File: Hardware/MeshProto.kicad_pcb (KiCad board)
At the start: 2 copper layers, 30.2 x 31.6 mm, 103 parts, among them P1 CONN_1, P10 CONN_1, P11 CONN_1, P12 CONN_1, P13 CONN_1, P14 CONN_1, P15 CONN_1, P16 CONN_1, P17 CONN_1, P18 CONN_1, P19 CONN_1, P2 CONN_1, P20 CONN_1, P21 CONN_1, P22 CONN_1, P23 CONN_1, P24 CONN_1, P25 CONN_1, P26 CONN_1, P27 CONN_1, P28 CONN_1, P29 CONN_1, P3 CONN_1, P30 CONN_1, P31 CONN_1, P32 CONN_1, P33 CONN_1, P34 CONN_1, P35 CONN_1, P36 CONN_1, P37 CONN_1, P38 CONN_1, P39 CONN_1, P4 CONN_1, P40 CONN_1, P41 CONN_1, P42 CONN_1, P43 CONN_1, P44 CONN_1, P45 CONN_1, P46 CONN_1, P47 CONN_1, P48 CONN_1, P49 CONN_1, P5 CONN_1, P50 CONN_1, P51 CONN_1, P52 CONN_1, P53 CONN_1, P54 CONN_1, P55 CONN_1, P56 CONN_1, P57 CONN_1, P58 CONN_1, P59 CONN_1, P6 CONN_1, P60 CONN_1, P61 CONN_1, P62 CONN_1, P63 CONN_1, P64 CONN_1, P65 CONN_1, P66 CONN_1, P67 CONN_1, P68 CONN_1, P69 CONN_1, P7 CONN_1, P70 CONN_1, P71 CONN_1, P72 CONN_1, P73 CONN_1, P74 CONN_1, P75 CONN_1, P76 CONN_1, P77 CONN_1, P78 CONN_1, P79 CONN_1, P8 CONN_1, P80 CONN_1, P81 CONN_1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

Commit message: Further minor changes.
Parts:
- moved SW1 3.82 mm to (134.7, 113.0), turned to 90 degrees
- moved P82 0.95 mm to (134.7, 108.3)
- moved P81 0.09 mm to (134.7, 106.7)
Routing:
- net N-0000052: track 8.81 -> 7.91 mm
- net GND: track 52.6 -> 53.5 mm
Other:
- board text added: "MeshProto v1.0 ©David Chanter, Bob Powers, Andy Gelme"
- board text added: "Reset"
- board text added: "This Way"
- board text removed: "MeshProto v1.0 © David Chanter, Bob Powers, Andy Gelme"
- board text removed: "This Way Up"
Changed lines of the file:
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@@
-(kicad_pcb (version 3) (host pcbnew "(2013-11-13 BZR 4466)-product")
+(kicad_pcb (version 3) (host pcbnew "(2013-11-20 BZR 4495)-product")
   (general
     (links 36)
-    (no_connects 1)
-    (area 131.413229 96.5166 165.135343 130.6954)
+    (no_connects 0)
+    (area 129.261801 96.5166 165.135343 130.6954)
     (thickness 1.6)
-    (drawings 31)
+    (drawings 32)
     (tracks 80)
     (zones 0)
@@
     (18 B.Paste user)
     (19 F.Paste user)
-    (20 B.SilkS user)
+    (20 B.SilkS user hide)
     (21 F.SilkS user)
     (22 B.Mask user)
@@
   )
   (setup
-    (last_trace_width 0.3048)
+    (last_trace_width 0.2032)
     (user_trace_width 0.3048)
     (trace_clearance 0.2032)
@@
   )
   (module _MT_TC007-TactileSwitch (layer F.Cu)
-    (at 134.71 116.82 270)
-    (fp_text reference SW1 (at -2.04 0 360) (layer F.SilkS)
+    (at 134.71 113.004 90)
+    (fp_text reference SW1 (at -2.04 0 180) (layer F.SilkS)
       (effects (font (size 0.75 0.75) (thickness 0.15)))
     )
-    (fp_text value SPST (at -0.01 -2.42 270) (layer F.SilkS) hide
+    (fp_text value SPST (at -0.01 -2.42 90) (layer F.SilkS) hide
       (effects (font (size 1.5 1.5) (thickness 0.15)))
     )
@@
     (fp_line (start -1.95 -1.45) (end 1.95 -1.45) (layer F.SilkS) (width 0.15))
     (fp_line (start 1.95 -1.45) (end 1.95 -0.73) (layer F.SilkS) (width 0.15))
-    (pad 1 smd rect (at -2.05 0 270) (size 0.9 1.3) (layers F.Cu F.Paste F.Mask)
+    (pad 1 smd rect (at -2.05 0 90) (size 0.9 1.3) (layers F.Cu F.Paste F.Mask)
       (net 3 N-0000052))
-    (pad 2 smd rect (at 2.05 0 270) (size 0.9 1.3) (layers F.Cu F.Paste F.Mask)
+    (pad 2 smd rect (at 2.05 0 90) (size 0.9 1.3) (layers F.Cu F.Paste F.Mask)
       (net 2 GND))
-    (pad "" thru_hole rect (at 0 0.9 270) (size 0.7 0.7) (drill 0.7) (layers *.Cu *.Mask F.SilkS))
-    (pad "" thru_hole rect (at -0.01 -0.9 270) (size 0.7 0.7) (drill 0.7) (layers *.Cu *.Mask F.SilkS))
-  )
-  (module _MP_1Pin (layer F.Cu)
-    (at 134.62 106.68)
+    (pad "" thru_hole rect (at 0 0.9 90) (size 0.7 0.7) (drill 0.7) (layers *.Cu *.Mask F.SilkS))
+    (pad "" thru_hole rect (at -0.01 -0.9 90) (size 0.7 0.7) (drill 0.7) (layers *.Cu *.Mask F.SilkS))
+  )
+  (module _MP_1Pin (layer F.Cu)
+    (at 134.71 106.68)
     (fp_text reference P81 (at 0 0) (layer F.SilkS) hide
       (effects (font (size 1 1) (thickness 0.15)))
@@
       (effects (font (size 1 1) (thickness 0.15)))
     )
-    (pad 1 thru_hole circle (at 0 0) (size 1.85928 1.85928) (drill 0.8128) (layers *.Cu *.Mask F.SilkS)
+    (pad 1 thru_hole circle (at 0 -0.946) (size 1.85928 1.85928) (drill 0.8128) (layers *.Cu *.Mask F.SilkS)
       (net 1 BAT+))
   )
   (module _MP_1Pin (layer F.Cu)
-    (at 134.62 109.22)
+    (at 134.71 108.274)
     (fp_text reference P82 (at 0 0) (layer F.SilkS) hide
       (effects (font (size 1 1) (thickness 0.15)))
@@
       (xy -0.75692 1.12268)) (layer F.SilkS) (width 0.00254))
   )
-  (gr_text meshthing.com (at 162.052 113.538 90) (layer B.SilkS)
-    (effects (font (size 1.5 1.5) (thickness 0.3)) (justify mirror))
-  )
-  (gr_text "MeshProto v1.0\n© David Chanter, Bob Powers,\nAndy Gelme" (at 161.3408 117.5766 90) (layer F.SilkS)
+  (gr_text Reset (at 134.71 116.11) (layer F.SilkS)
+    (effects (font (size 0.5 0.5) (thickness 0.125)))
+  )
+  (gr_text meshthing.com (at 162.08 115.87 90) (layer F.SilkS)
+    (effects (font (size 1.5 1.5) (thickness 0.3)))
+  )
+  (gr_text "MeshProto v1.0\n©David Chanter, Bob Powers,\nAndy Gelme" (at 161.3408 103.62 90) (layer B.SilkS)
+    (effects (font (size 0.5 0.5) (thickness 0.1)) (justify left mirror))
+  )
+  (gr_text ↑ (at 162.8394 106.35) (layer F.SilkS)
+    (effects (font (size 1.5 1.5) (thickness 0.3)))
+  )
+  (gr_line (start 162.56 103.6938) (end 161.8742 103.6938) (angle 90) (layer F.SilkS) (width 0.2))
+  (gr_line (start 161.3662 104.2018) (end 161.8234 103.7446) (angle 90) (layer F.SilkS) (width 0.2))
+  (gr_line (start 161.3662 105.4718) (end 161.3662 104.2018) (angle 90) (layer F.SilkS) (width 0.2))
+  (gr_line (start 163.0426 105.4718) (end 161.3662 105.4718) (angle 90) (layer F.SilkS) (width 0.2))
+  (gr_line (start 163.0426 104.1764) (end 163.0426 105.4718) (angle 90) (layer F.SilkS) (width 0.2))
+  (gr_line (start 162.56 103.6938) (end 163.0426 104.1764) (angle 90) (layer F.SilkS) (width 0.2))
+  (gr_text "This\nWay" (at 161.6456 106.45) (layer F.SilkS)
     (effects (font (size 0.5 0.5) (thickness 0.1)))
   )
-  (gr_text ↑ (at 162.8394 107.4928) (layer F.SilkS)
-    (effects (font (size 1.5 1.5) (thickness 0.3)))
-  )
-  (gr_line (start 162.56 104.0638) (end 161.8742 104.0638) (angle 90) (layer F.SilkS) (width 0.2))
-  (gr_line (start 161.3662 104.5718) (end 161.8234 104.1146) (angle 90) (layer F.SilkS) (width 0.2))
-  (gr_line (start 161.3662 105.8418) (end 161.3662 104.5718) (angle 90) (layer F.SilkS) (width 0.2))
-  (gr_line (start 163.0426 105.8418) (end 161.3662 105.8418) (angle 90) (layer F.SilkS) (width 0.2))
-  (gr_line (start 163.0426 104.5464) (end 163.0426 105.8418) (angle 90) (layer F.SilkS) (width 0.2))
-  (gr_line (start 162.56 104.0638) (end 163.0426 104.5464) (angle 90) (layer F.SilkS) (width 0.2))
-  (gr_text "This\nWay\nUp" (at 161.6456 106.7562) (layer F.SilkS)
+  (gr_text GND (at 134.71 109.75) (layer F.SilkS)
     (effects (font (size 0.5 0.5) (thickness 0.1)))
   )
-  (gr_text GND (at 134.493 110.998) (layer F.SilkS)
+  (gr_text 3v3 (at 134.71 104.25) (layer F.SilkS)
     (effects (font (size 0.5 0.5) (thickness 0.1)))
   )
-  (gr_text 3v3 (at 134.62 104.902) (layer F.SilkS)
-    (effects (font (size 0.5 0.5) (thickness 0.1)))
-  )
-  (gr_text 3v3 (at 139.954 100.076) (layer F.SilkS)
+  (gr_text 3v3 (at 139.7 100.076) (layer F.SilkS)
     (effects (font (size 0.5 0.5) (thickness 0.1)))
   )
@@
   (gr_line (start 138.938 126.746) (end 141.097 126.746) (angle 90) (layer F.SilkS) (width 0.2))
   (gr_line (start 140.97 129.159) (end 138.938 129.159) (angle 90) (layer F.SilkS) (width 0.2))
-  (gr_text GND (at 139.827 128.016) (layer F.SilkS)
+  (gr_text GND (at 139.7 128.016) (layer F.SilkS)
     (effects (font (size 0.5 0.5) (thickness 0.1)))
   )
@@
   (gr_line (start 133.4 129.35) (end 133.4 97.75) (angle 90) (layer Edge.Cuts) (width 0.1))
   (gr_line (start 163.6 129.35) (end 133.4 129.35) (angle 90) (layer Edge.Cuts) (width 0.1))
-  (segment (start 137.5 105.004) (end 136.296 105.004) (width 0.3048) (layer F.Cu) (net 1))
-  (segment (start 136.296 105.004) (end 134.62 106.68) (width 0.3048) (layer F.Cu) (net 1))
+  (segment (start 137.5 105.004) (end 135.44 105.004) (width 0.3048) (layer F.Cu) (net 1))
+  (segment (start 135.44 105.004) (end 134.71 105.734) (width 0.3048) (layer F.Cu) (net 1))
   (segment (start 137.5 105.004) (end 137.5 104.816) (width 0.3048) (layer F.Cu) (net 1))
   (segment (start 137.5 104.816) (end 139.7 102.616) (width 0.3048) (layer F.Cu) (net 1))
@@
   (segment (start 149.86 100.076) (end 152.4 100.076) (width 0.2032) (layer F.Cu) (net 1))
   (segment (start 152.4 100.076) (end 154.94 100.076) (width 0.2032) (layer F.Cu) (net 1))
-  (segment (start 134.62 109.22) (end 134.7 109.3) (width 0.3048) (layer B.Cu) (net 2))
+  (segment (start 134.71 108.274) (end 134.71 110.954) (width 0.3048) (layer F.Cu) (net 2))
+  (segment (start 142.24 128.016) (end 144.78 128.016) (width 0.3048) (layer F.Cu) (net 2))
+  (segment (start 134.7 109.97) (end 134.7 108.354) (width 0.3048) (layer B.Cu) (net 2))
+  (segment (start 134.7 108.354) (end 134.62 108.274) (width 0.3048) (layer B.Cu) (net 2))
   (segment (start 134.7 120.204) (end 137.5 123.004) (width 0.3048) (layer B.Cu) (net 2))
-  (segment (start 134.7 109.3) (end 134.7 120.204) (width 0.3048) (layer B.Cu) (net 2))
+  (segment (start 134.7 109.97) (end 134.7 120.204) (width 0.3048) (layer B.Cu) (net 2))
   (segment (start 139.7 125.476) (end 142.24 128.016) (width 0.3048) (layer F.Cu) (net 2))
   (segment (start 142.24 128.016) (end 154.94 128.016) (width 0.3048) (layer F.Cu) (net 2))
   (segment (start 137.5 123.004) (end 137.5 123.276) (width 0.3048) (layer F.Cu) (net 2))
   (segment (start 137.5 123.276) (end 139.7 125.476) (width 0.3048) (layer F.Cu) (net 2))
-  (segment (start 134.71 118.87) (end 134.71 120.214) (width 0.3048) (layer F.Cu) (net 2))
-  (segment (start 134.71 120.214) (end 137.5 123.004) (width 0.3048) (layer F.Cu) (net 2))
   (segment (start 142.24 128.016) (end 147.32 128.016) (width 0.2032) (layer F.Cu) (net 2))
   (segment (start 147.32 128.016) (end 149.86 128.016) (width 0.2032) (layer F.Cu) (net 2))
   (segment (start 149.86 128.016) (end 152.4 128.016) (width 0.2032) (layer F.Cu) (net 2))
   (segment (start 152.4 128.016) (end 154.94 128.016) (width 0.2032) (layer F.Cu) (net 2))
+  (segment (start 137.5 113.004) (end 135.45 115.054) (width 0.3048) (layer F.Cu) (net 3))
+  (segment (start 135.45 115.054) (end 134.71 115.054) (width 0.3048) (layer F.Cu) (net 3))
   (segment (start 139.7 112.776) (end 139.472 113.004) (width 0.3048) (layer F.Cu) (net 3))
   (segment (start 139.472 113.004) (end 137.5 113.004) (width 0.3048) (layer F.Cu) (net 3))
-  (segment (start 134.71 114.77) (end 136.476 113.004) (width 0.3048) (layer F.Cu) (net 3))
-  (segment (start 136.476 113.004) (end 137.5 113.004) (width 0.3048) (layer F.Cu) (net 3))
   (segment (start 137.5 113.004) (end 139.472 113.004) (width 0.2032) (layer F.Cu) (net 3))
-  (segment (start 137.5 113.004) (end 136.476 113.004) (width 0.2032) (layer F.Cu) (net 3))
   (segment (start 139.7 117.856) (end 138.848 117.004) (width 0.3048) (layer F.Cu) (net 4))
   (segment (start 138.848 117.004) (end 137.5 117.004) (width 0.3048) (layer F.Cu) (net 4))

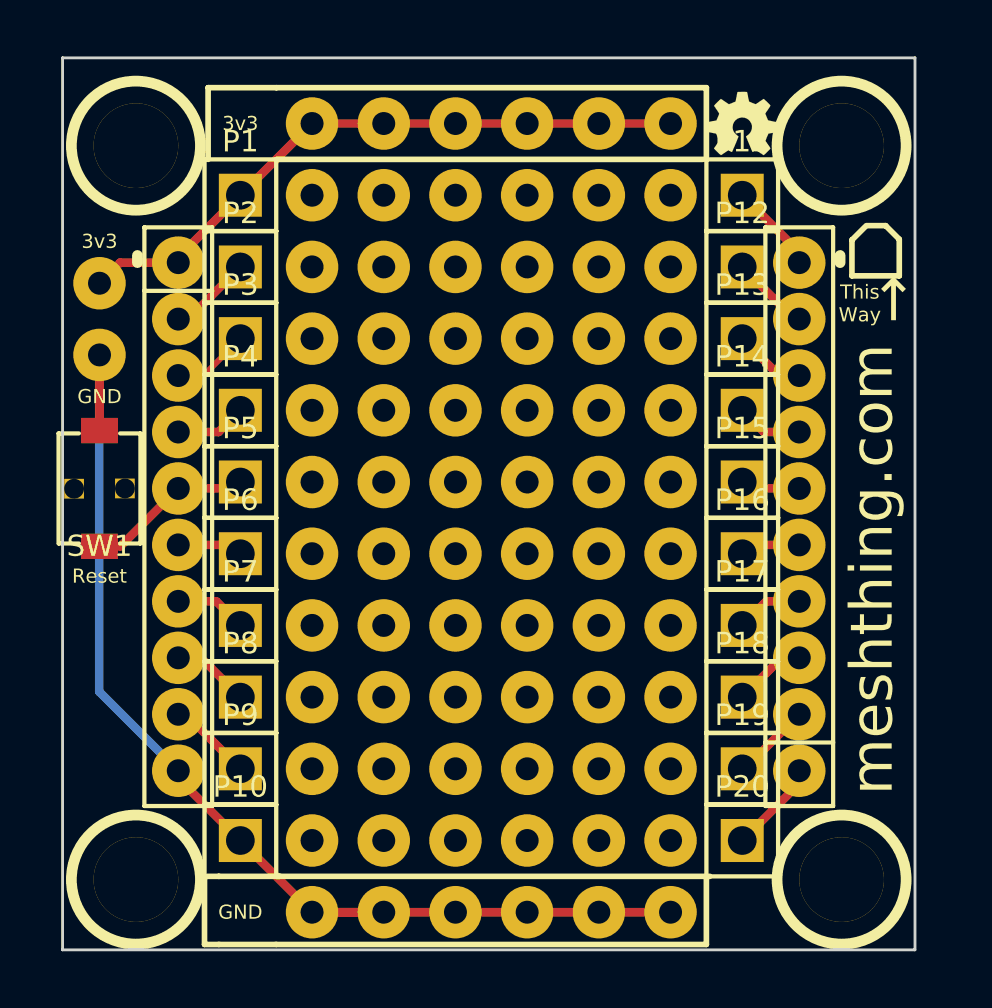
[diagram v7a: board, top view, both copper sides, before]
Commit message: Cleaned up silk, added license.
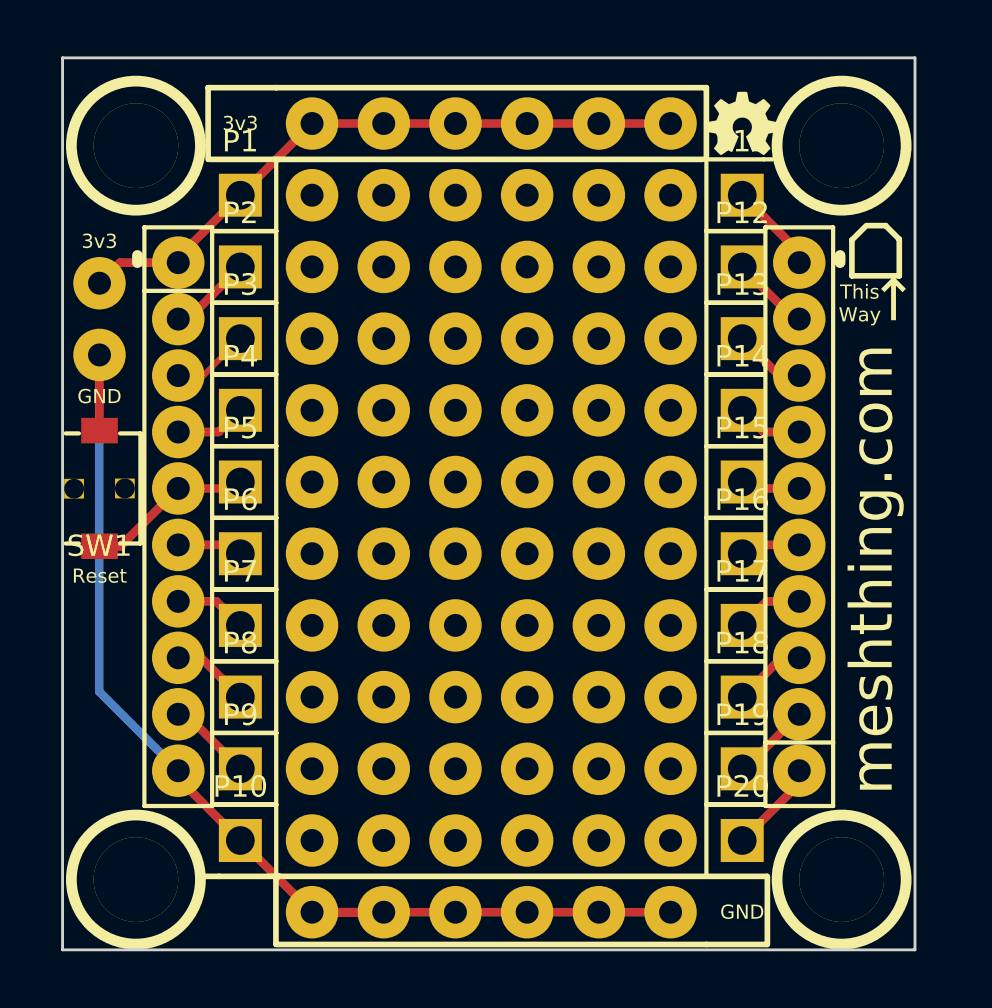
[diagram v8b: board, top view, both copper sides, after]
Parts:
- P1, P10, P2, P3, P4, P5, P6, P7, P8, P9: footprint PIN_ARRAY_1 -> _MP_:_MP_PIN_ARRAY_1-Left
- P11, P12, P13, P14, P15, P16, P17, P18, P19, P20: footprint PIN_ARRAY_1 -> _MP_:_MP_PIN_ARRAY_1-Right
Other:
- board text added: "OpenHardware Under TAPR OHL tapr.org/OHL"
